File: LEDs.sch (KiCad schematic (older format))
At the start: 18 parts

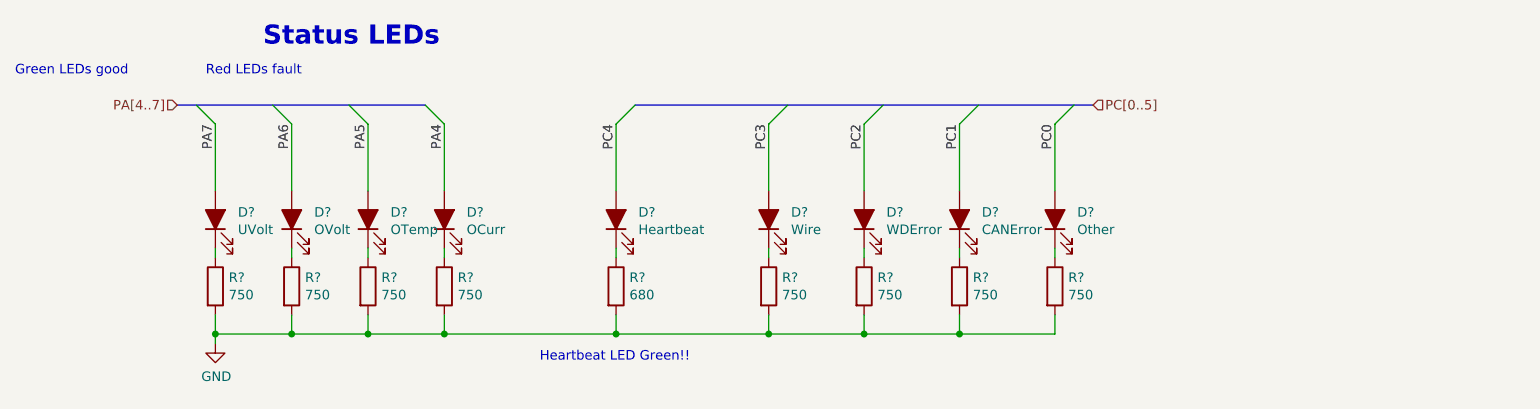
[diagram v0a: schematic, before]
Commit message: Adds logic analyzer points and LEDs
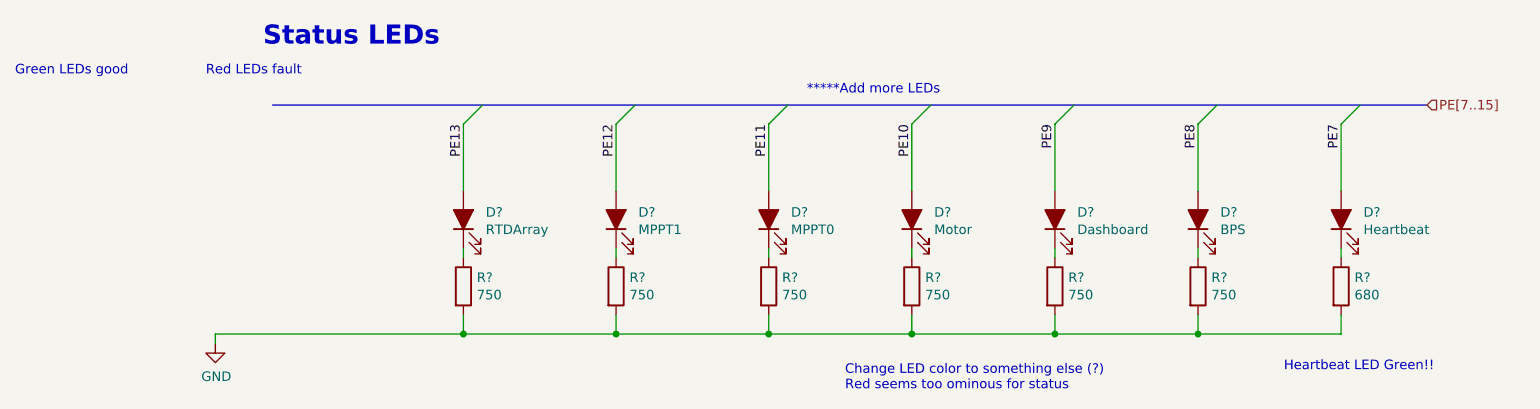
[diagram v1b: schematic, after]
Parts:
- removed D?: UVolt, LED_SMD:LED_0805_2012Metric, symbol Device:LED_ALT
- removed D?: OVolt, LED_SMD:LED_0805_2012Metric, symbol Device:LED_ALT
- removed D?: OTemp, LED_SMD:LED_0805_2012Metric, symbol Device:LED_ALT
- removed D?: OCurr, LED_SMD:LED_0805_2012Metric, symbol Device:LED_ALT
- removed R? (x4): 750, Resistor_SMD:R_0805_2012Metric, symbol Device:R
- added D?: RTDArray, LED_SMD:LED_0805_2012Metric, symbol Device:LED_ALT
- added D?: MPPT1, LED_SMD:LED_0805_2012Metric, symbol Device:LED_ALT
- added R? (x2): 750, Resistor_SMD:R_0805_2012Metric, symbol Device:R
- D?: value Wire -> MPPT0
- D?: value CANError -> Dashboard
- D?: value WDError -> Motor
- D?: value Other -> BPS
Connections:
- net GND: now also R?.2, R?.2
- net PC0 renamed PE8
- net PC1 renamed PE9
- net PC2 renamed PE10
- net PC3 renamed PE11
- net PC4 renamed PE7
- new net: D?.1 (K), R?.1 (x2)
- new net PE12: D?.2 (A)
- new net PE13: D?.2 (A)
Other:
- note added: "*****Add more LEDs"
- note added: "Change LED color to something else (?)\nRed seems too ominous for status"
- moved on the sheet: D?, R?

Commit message: Initial layout of the Telemtry board.
The ethernet interface needs more work.
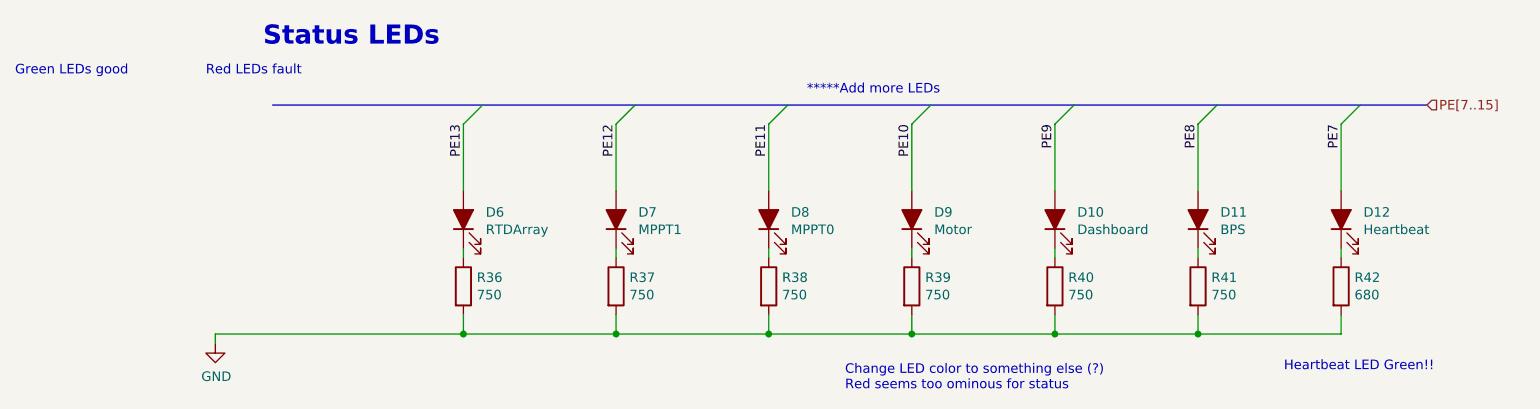
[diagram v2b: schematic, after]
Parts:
- gave numbers to parts that had none: 14
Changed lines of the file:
@@
 PE[7..15]
 $Comp
-L Device:LED_ALT D?
+L Device:LED_ALT D12
 U 1 1 5C3C069F
 P 9600 3100
-F 0 "D?" V 9638 2983 50  0000 R CNN
+F 0 "D12" V 9638 2983 50  0000 R CNN
 F 1 "Heartbeat" V 9547 2983 50  0000 R CNN
 F 2 "LED_SMD:LED_0805_2012Metric" H 9600 3100 50  0001 C CNN
@@
 $EndComp
 $Comp
-L Device:R R?
+L Device:R R42
 U 1 1 5C3C06D9
 P 9600 3450
-F 0 "R?" H 9670 3496 50  0000 L CNN
+F 0 "R42" H 9670 3496 50  0000 L CNN
 F 1 "680" H 9670 3405 50  0000 L CNN
 F 2 "Resistor_SMD:R_0805_2012Metric" V 9530 3450 50  0001 C CNN
@@
 	6600 3700 6600 3600
 $Comp
-L Device:R R?
+L Device:R R38
 U 1 1 5C3C0718
 P 6600 3450
-F 0 "R?" H 6670 3496 50  0000 L CNN
+F 0 "R38" H 6670 3496 50  0000 L CNN
 F 1 "750" H 6670 3405 50  0000 L CNN
 F 2 "Resistor_SMD:R_0805_2012Metric" V 6530 3450 50  0001 C CNN
@@
 	6600 3250 6600 3300
 $Comp
-L power:GND #PWR?
+L power:GND #PWR0176
 U 1 1 5C3C0722
 P 3700 3750
-F 0 "#PWR?" H 3700 3500 50  0001 C CNN
+F 0 "#PWR0176" H 3700 3500 50  0001 C CNN
 F 1 "GND" H 3705 3577 50  0000 C CNN
 F 2 "" H 3700 3750 50  0001 C CNN
@@
 	7350 3700 7350 3600
 $Comp
-L Device:R R?
+L Device:R R39
 U 1 1 5C6CF943
 P 7350 3450
-F 0 "R?" H 7420 3496 50  0000 L CNN
+F 0 "R39" H 7420 3496 50  0000 L CNN
 F 1 "750" H 7420 3405 50  0000 L CNN
 F 2 "Resistor_SMD:R_0805_2012Metric" V 7280 3450 50  0001 C CNN
@@
 	8100 3700 8100 3600
 $Comp
-L Device:R R?
+L Device:R R40
 U 1 1 5C585DC3
 P 8100 3450
-F 0 "R?" H 8170 3496 50  0000 L CNN
+F 0 "R40" H 8170 3496 50  0000 L CNN
 F 1 "750" H 8170 3405 50  0000 L CNN
 F 2 "Resistor_SMD:R_0805_2012Metric" V 8030 3450 50  0001 C CNN
@@
 	9600 2950 9600 2600
 $Comp
-L Device:LED_ALT D?
+L Device:LED_ALT D11
 U 1 1 5F16CED0
 P 8850 3100
-F 0 "D?" V 8888 2983 50  0000 R CNN
+F 0 "D11" V 8888 2983 50  0000 R CNN
 F 1 "BPS" V 8797 2983 50  0000 R CNN
 F 2 "LED_SMD:LED_0805_2012Metric" H 8850 3100 50  0001 C CNN
@@
 $EndComp
 $Comp
-L Device:R R?
+L Device:R R41
 U 1 1 5F16CED6
 P 8850 3450
-F 0 "R?" H 8920 3496 50  0000 L CNN
+F 0 "R41" H 8920 3496 50  0000 L CNN
 F 1 "750" H 8920 3405 50  0000 L CNN
 F 2 "Resistor_SMD:R_0805_2012Metric" V 8780 3450 50  0001 C CNN
@@
 	8850 3700 8850 3600
 $Comp
-L Device:LED_ALT D?
+L Device:LED_ALT D8
 U 1 1 5C3C070F
 P 6600 3100
-F 0 "D?" V 6638 2983 50  0000 R CNN
+F 0 "D8" V 6638 2983 50  0000 R CNN
 F 1 "MPPT0" V 6547 2983 50  0000 R CNN
 F 2 "LED_SMD:LED_0805_2012Metric" H 6600 3100 50  0001 C CNN
@@
 $EndComp
 $Comp
-L Device:LED_ALT D?
+L Device:LED_ALT D9
 U 1 1 5C6CF93B
 P 7350 3100
-F 0 "D?" V 7388 2983 50  0000 R CNN
+F 0 "D9" V 7388 2983 50  0000 R CNN
 F 1 "Motor" V 7297 2983 50  0000 R CNN
 F 2 "LED_SMD:LED_0805_2012Metric" H 7350 3100 50  0001 C CNN
@@
 $EndComp
 $Comp
-L Device:LED_ALT D?
+L Device:LED_ALT D10
 U 1 1 5C585DBB
 P 8100 3100
-F 0 "D?" V 8138 2983 50  0000 R CNN
+F 0 "D10" V 8138 2983 50  0000 R CNN
 F 1 "Dashboard" V 8047 2983 50  0000 R CNN
 F 2 "LED_SMD:LED_0805_2012Metric" H 8100 3100 50  0001 C CNN
@@
 	5000 3700 5000 3600
 $Comp
-L Device:R R?
+L Device:R R36
 U 1 1 5FE2D5D7
 P 5000 3450
-F 0 "R?" H 5070 3496 50  0000 L CNN
+F 0 "R36" H 5070 3496 50  0000 L CNN
 F 1 "750" H 5070 3405 50  0000 L CNN
 F 2 "Resistor_SMD:R_0805_2012Metric" V 4930 3450 50  0001 C CNN
@@
 	5100 2500 5000 2600
 $Comp
-L Device:LED_ALT D?
+L Device:LED_ALT D6
 U 1 1 5FE2D5E1
 P 5000 3100
-F 0 "D?" V 5038 2983 50  0000 R CNN
+F 0 "D6" V 5038 2983 50  0000 R CNN
 F 1 "RTDArray" V 4947 2983 50  0000 R CNN
 F 2 "LED_SMD:LED_0805_2012Metric" H 5000 3100 50  0001 C CNN
@@
 	5800 3700 5800 3600
 $Comp
-L Device:R R?
+L Device:R R37
 U 1 1 5FEA8B72
 P 5800 3450
-F 0 "R?" H 5870 3496 50  0000 L CNN
+F 0 "R37" H 5870 3496 50  0000 L CNN
 F 1 "750" H 5870 3405 50  0000 L CNN
 F 2 "Resistor_SMD:R_0805_2012Metric" V 5730 3450 50  0001 C CNN
@@
 	5900 2500 5800 2600
 $Comp
-L Device:LED_ALT D?
+L Device:LED_ALT D7
 U 1 1 5FEA8B7C
 P 5800 3100
-F 0 "D?" V 5838 2983 50  0000 R CNN
+F 0 "D7" V 5838 2983 50  0000 R CNN
 F 1 "MPPT1" V 5747 2983 50  0000 R CNN
 F 2 "LED_SMD:LED_0805_2012Metric" H 5800 3100 50  0001 C CNN
